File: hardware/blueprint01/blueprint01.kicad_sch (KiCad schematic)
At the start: 3 parts, among them U1 TB6612FNG, U2 LM7805

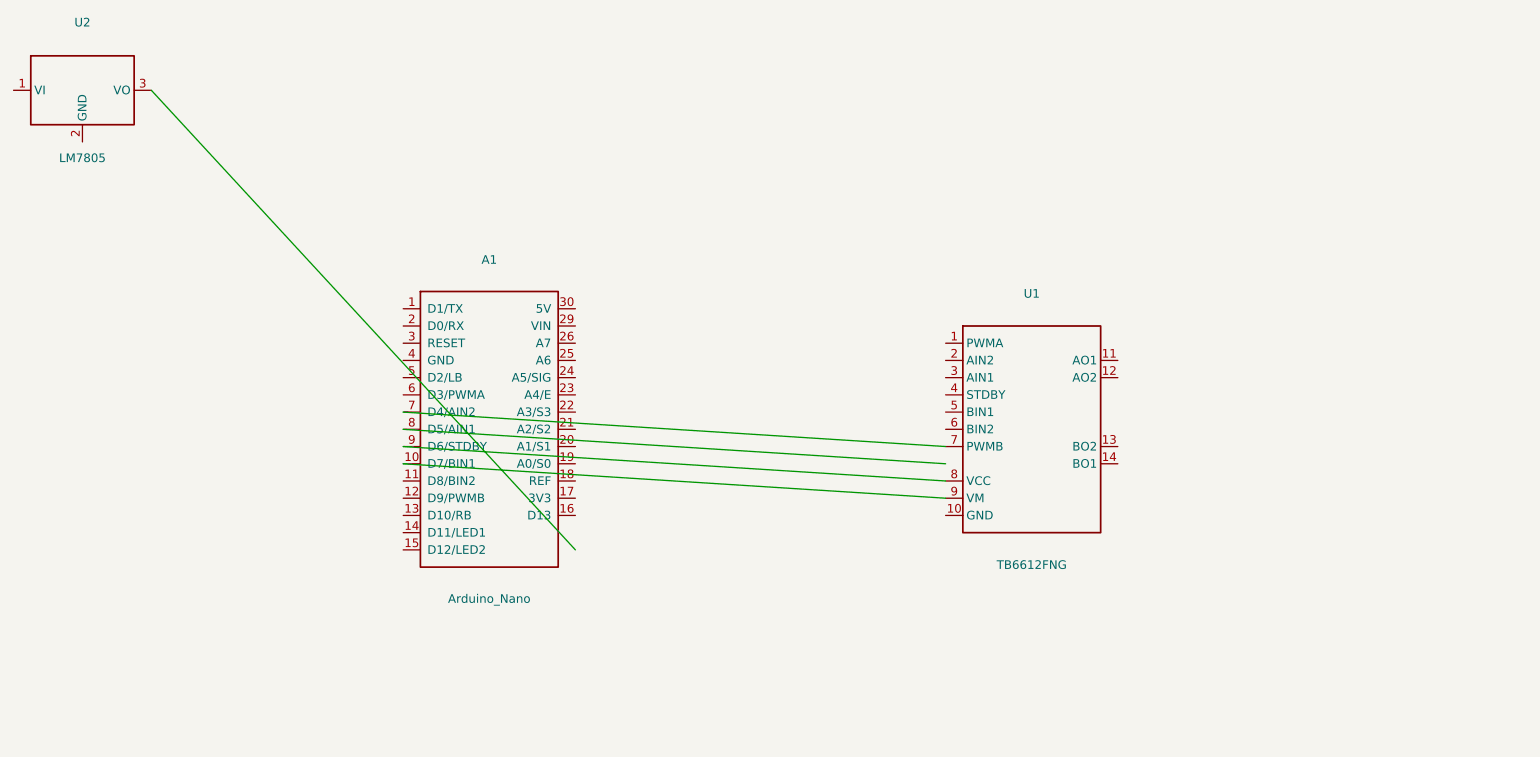
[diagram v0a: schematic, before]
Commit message: hardware: complete ARC16 schematic with all 16 IR LEDs, phototransistors, resistors, and MUX connections
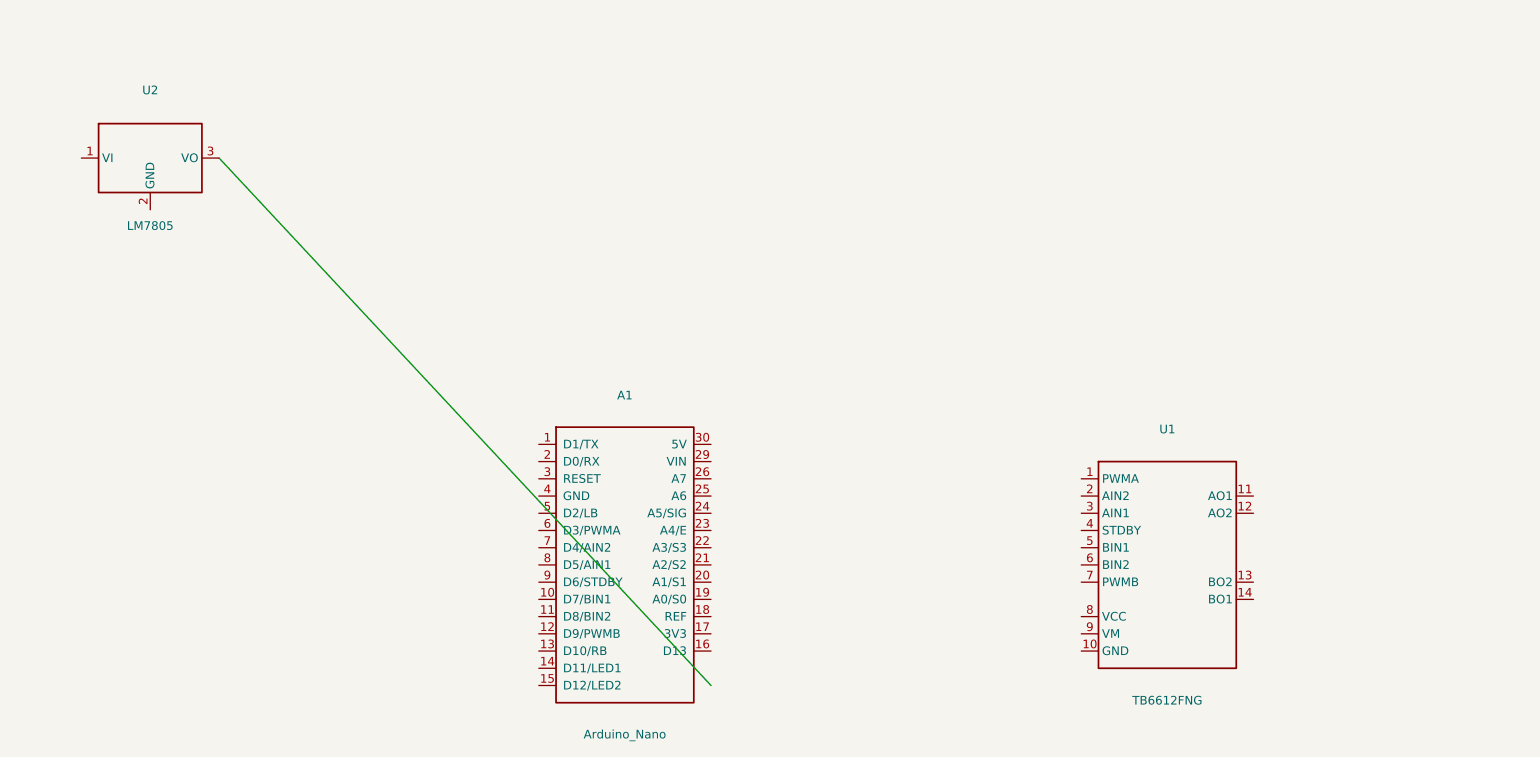
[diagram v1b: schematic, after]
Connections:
- net at A1.10 (D7/BIN1): no longer U1.9 (VM)
- net at A1.7 (D4/AIN2): no longer U1.7 (PWMB)
- net at A1.9 (D6/STDBY): no longer U1.8 (VCC)
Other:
- moved on the sheet: A1, U1, U2
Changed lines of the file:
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@@
 (kicad_sch (version 20230121) (generator "TechGeeks KiCad Generator")
-  (paper "A4")
+  (paper "A3")
   (title_block
     (title "Blueprint 01 - Robot Controller Board")
@@
     (comment 2 "Designed for Line Follower Robots")
   )
-  (symbol (lib_id "MCU_Module:Arduino_Nano") (at 100 100 0) (unit 1)
+  (symbol (lib_id "MCU_Module:Arduino_Nano") (at 120 120 0) (unit 1)
     (in_bom yes) (on_board yes)
-    (property "Reference" "A1" (at 100 75 0) (effects (font (size 1.27 1.27))))
-    (property "Value" "Arduino_Nano" (at 100 125 0) (effects (font (size 1.27 1.27))))
+    (property "Reference" "A1" (at 120 95 0) (effects (font (size 1.27 1.27))))
+    (property "Value" "Arduino_Nano" (at 120 145 0) (effects (font (size 1.27 1.27))))
   )
-  (symbol (lib_id "Driver_Motor:TB6612FNG") (at 180 100 0) (unit 1)
+  (symbol (lib_id "Driver_Motor:TB6612FNG") (at 200 120 0) (unit 1)
     (in_bom yes) (on_board yes)
-    (property "Reference" "U1" (at 180 80 0) (effects (font (size 1.27 1.27))))
-    (property "Value" "TB6612FNG" (at 180 120 0) (effects (font (size 1.27 1.27))))
+    (property "Reference" "U1" (at 200 100 0) (effects (font (size 1.27 1.27))))
+    (property "Value" "TB6612FNG" (at 200 140 0) (effects (font (size 1.27 1.27))))
   )
-  (symbol (lib_id "Regulator_Linear:LM7805") (at 40 50 0) (unit 1)
+  (symbol (lib_id "Regulator_Linear:LM7805") (at 50 60 0) (unit 1)
     (in_bom yes) (on_board yes)
-    (property "Reference" "U2" (at 40 40 0) (effects (font (size 1.27 1.27))))
-    (property "Value" "LM7805" (at 40 60 0) (effects (font (size 1.27 1.27))))
+    (property "Reference" "U2" (at 50 50 0) (effects (font (size 1.27 1.27))))
+    (property "Value" "LM7805" (at 50 70 0) (effects (font (size 1.27 1.27))))
   )
-  (wire (pts (xy 50.16 50) (xy 112.7 117.78)) (stroke (width 0) (type default)))
-  (wire (pts (xy 87.3 105.08) (xy 167.3 110.16)) (stroke (width 0) (type default)))
-  (wire (pts (xy 87.3 102.54) (xy 167.3 107.62)) (stroke (width 0) (type default)))
-  (wire (pts (xy 87.3 100) (xy 167.3 105.08)) (stroke (width 0) (type default)))
-  (wire (pts (xy 87.3 97.46) (xy 167.3 102.54)) (stroke (width 0) (type default)))
+  (wire (pts (xy 60.16 60) (xy 132.7 137.78)) (stroke (width 0) (type default)))
   (sheet_instances
     (path "/" (page "1"))

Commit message: hardware: clean visual schematic layout with net-label architecture for ARC16 16-channel array
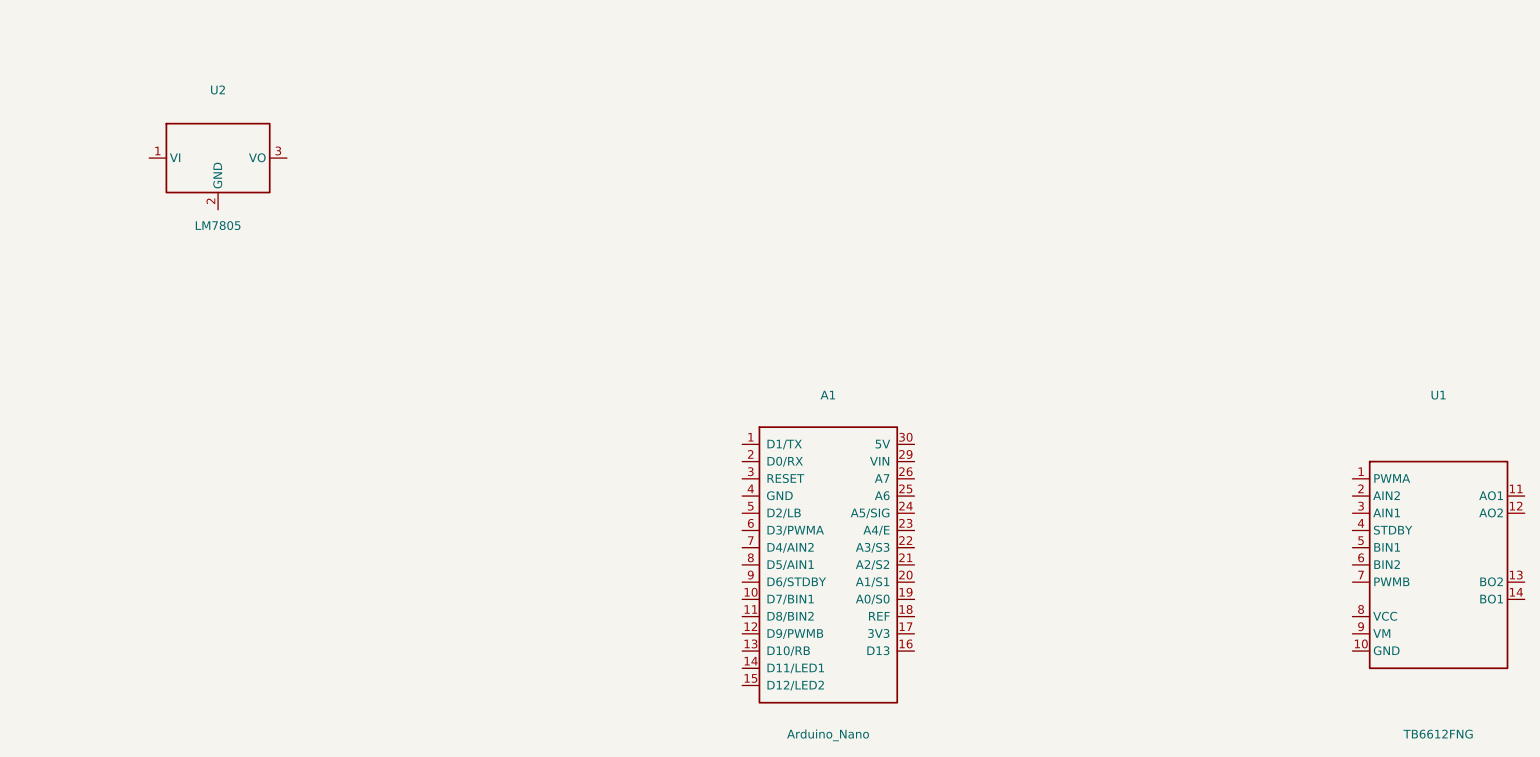
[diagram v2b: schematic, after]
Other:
- moved on the sheet: A1, U1, U2
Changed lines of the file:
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@@
     (comment 2 "Designed for Line Follower Robots")
   )
-  (symbol (lib_id "MCU_Module:Arduino_Nano") (at 120 120 0) (unit 1)
+  (symbol (lib_id "MCU_Module:Arduino_Nano") (at 150 120 0) (unit 1)
     (in_bom yes) (on_board yes)
-    (property "Reference" "A1" (at 120 95 0) (effects (font (size 1.27 1.27))))
-    (property "Value" "Arduino_Nano" (at 120 145 0) (effects (font (size 1.27 1.27))))
+    (property "Reference" "A1" (at 150 95 0) (effects (font (size 1.27 1.27))))
+    (property "Value" "Arduino_Nano" (at 150 145 0) (effects (font (size 1.27 1.27))))
   )
-  (symbol (lib_id "Driver_Motor:TB6612FNG") (at 200 120 0) (unit 1)
+  (symbol (lib_id "Driver_Motor:TB6612FNG") (at 240 120 0) (unit 1)
     (in_bom yes) (on_board yes)
-    (property "Reference" "U1" (at 200 100 0) (effects (font (size 1.27 1.27))))
-    (property "Value" "TB6612FNG" (at 200 140 0) (effects (font (size 1.27 1.27))))
+    (property "Reference" "U1" (at 240 95 0) (effects (font (size 1.27 1.27))))
+    (property "Value" "TB6612FNG" (at 240 145 0) (effects (font (size 1.27 1.27))))
   )
-  (symbol (lib_id "Regulator_Linear:LM7805") (at 50 60 0) (unit 1)
+  (symbol (lib_id "Regulator_Linear:LM7805") (at 60 60 0) (unit 1)
     (in_bom yes) (on_board yes)
-    (property "Reference" "U2" (at 50 50 0) (effects (font (size 1.27 1.27))))
-    (property "Value" "LM7805" (at 50 70 0) (effects (font (size 1.27 1.27))))
+    (property "Reference" "U2" (at 60 50 0) (effects (font (size 1.27 1.27))))
+    (property "Value" "LM7805" (at 60 70 0) (effects (font (size 1.27 1.27))))
   )
-  (wire (pts (xy 60.16 60) (xy 132.7 137.78)) (stroke (width 0) (type default)))
   (sheet_instances
     (path "/" (page "1"))
